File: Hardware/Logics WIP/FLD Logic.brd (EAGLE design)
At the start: 61.6 x 33 mm, 82 parts

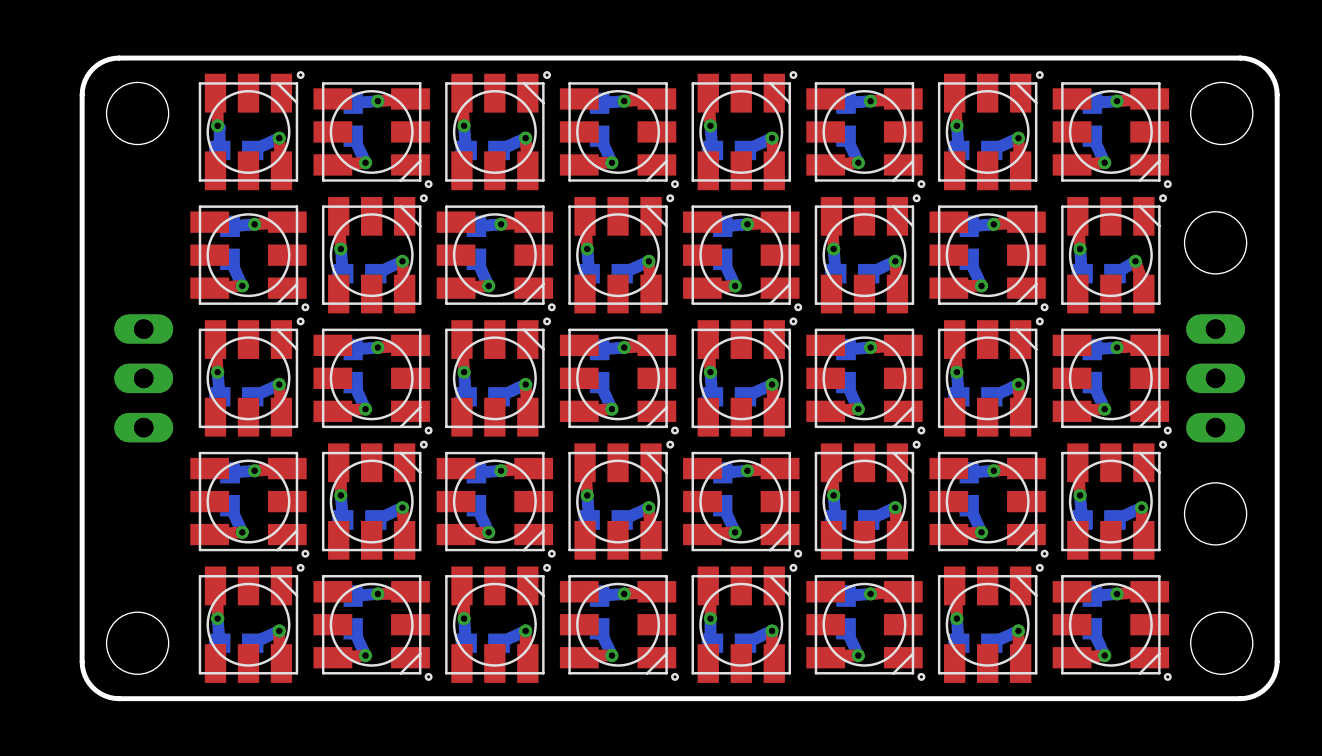
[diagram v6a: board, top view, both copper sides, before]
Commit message: 
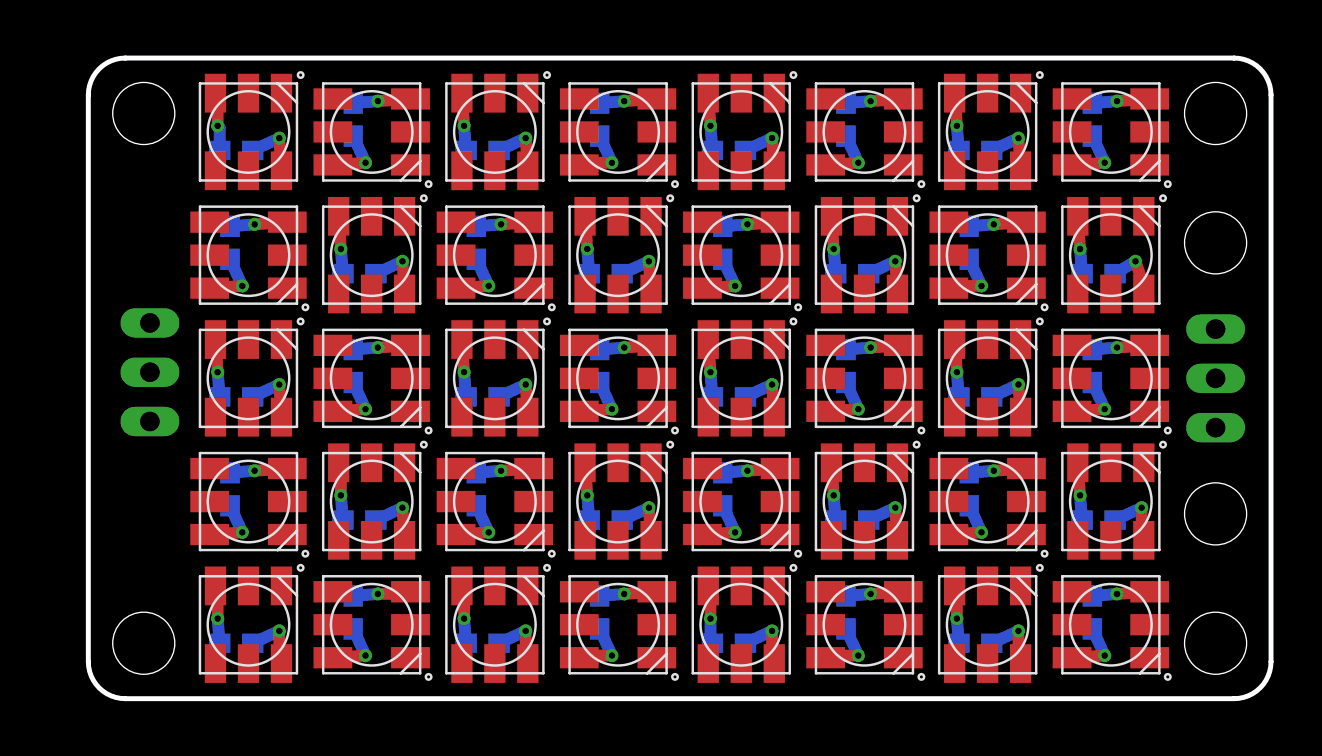
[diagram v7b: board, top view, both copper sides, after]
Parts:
- added U$1: (no value), rseries:RSERIES-OSHW-LOGO-SMALL
- moved OUT 0.45 mm to (3.49, 16.8)
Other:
- board size 61.6 x 33 mm -> 61 x 33 mm
- board text added: "`VULCAN' FRONT LOGIC DISPLAY 2013-08-28"
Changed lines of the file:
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@@
 <setting verticaltext="up"/>
 </settings>
-<grid distance="0.025" unitdist="inch" unit="inch" style="lines" multiple="1" display="yes" altdistance="0.025" altunitdist="inch" altunit="inch"/>
+<grid distance="0.0125" unitdist="inch" unit="inch" style="lines" multiple="1" display="yes" altdistance="0.025" altunitdist="inch" altunit="inch"/>
 <layers>
 <layer number="1" name="Top" color="4" fill="1" visible="yes" active="yes"/>
@@
 <layer number="37" name="tTest" color="7" fill="1" visible="yes" active="yes"/>
 <layer number="38" name="bTest" color="7" fill="1" visible="yes" active="yes"/>
+<layer number="39" name="tKeepout" color="4" fill="11" visible="yes" active="yes"/>
 <layer number="40" name="bKeepout" color="1" fill="11" visible="yes" active="yes"/>
+<layer number="41" name="tRestrict" color="4" fill="10" visible="yes" active="yes"/>
+<layer number="42" name="bRestrict" color="1" fill="10" visible="yes" active="yes"/>
+<layer number="43" name="vRestrict" color="2" fill="10" visible="yes" active="yes"/>
 <layer number="44" name="Drills" color="7" fill="1" visible="yes" active="yes"/>
 <layer number="45" name="Holes" color="7" fill="1" visible="yes" active="yes"/>
@@
 <layer number="106" name="bPlate" color="7" fill="1" visible="yes" active="yes"/>
 <layer number="107" name="Crop" color="7" fill="1" visible="yes" active="yes"/>
+<layer number="108" name="fp8" color="7" fill="1" visible="yes" active="yes"/>
+<layer number="109" name="fp9" color="7" fill="1" visible="yes" active="yes"/>
+<layer number="110" name="fp0" color="7" fill="1" visible="yes" active="yes"/>
+<layer number="111" name="LPC17xx" color="7" fill="1" visible="yes" active="yes"/>
 <layer number="112" name="tSilk" color="7" fill="1" visible="yes" active="yes"/>
 <layer number="116" name="Patch_BOT" color="9" fill="4" visible="yes" active="yes"/>
+<layer number="121" name="_tsilk" color="7" fill="1" visible="yes" active="yes"/>
+<layer number="122" name="_bsilk" color="7" fill="1" visible="yes" active="yes"/>
+<layer number="123" name="tTestmark" color="7" fill="1" visible="yes" active="yes"/>
+<layer number="124" name="bTestmark" color="7" fill="1" visible="yes" active="yes"/>
+<layer number="125" name="_tNames" color="7" fill="1" visible="yes" active="yes"/>
+<layer number="131" name="tAdjust" color="7" fill="1" visible="yes" active="yes"/>
+<layer number="132" name="bAdjust" color="7" fill="1" visible="yes" active="yes"/>
+<layer number="144" name="Drill_legend" color="7" fill="1" visible="yes" active="yes"/>
 <layer number="150" name="Notes" color="7" fill="1" visible="yes" active="yes"/>
+<layer number="151" name="HeatSink" color="7" fill="1" visible="yes" active="yes"/>
 <layer number="153" name="FabDoc1" color="6" fill="1" visible="no" active="no"/>
 <layer number="154" name="FabDoc2" color="2" fill="1" visible="no" active="no"/>
 <layer number="155" name="FabDoc3" color="7" fill="15" visible="no" active="no"/>
+<layer number="199" name="Contour" color="7" fill="1" visible="yes" active="yes"/>
+<layer number="200" name="200bmp" color="1" fill="10" visible="yes" active="yes"/>
+<layer number="201" name="201bmp" color="2" fill="10" visible="yes" active="yes"/>
+<layer number="202" name="202bmp" color="3" fill="10" visible="yes" active="yes"/>
+<layer number="203" name="203bmp" color="4" fill="10" visible="yes" active="yes"/>
+<layer number="204" name="204bmp" color="5" fill="10" visible="yes" active="yes"/>
+<layer number="205" name="205bmp" color="6" fill="10" visible="yes" active="yes"/>
+<layer number="206" name="206bmp" color="7" fill="10" visible="yes" active="yes"/>
+<layer number="207" name="207bmp" color="8" fill="10" visible="yes" active="yes"/>
+<layer number="208" name="208bmp" color="9" fill="10" visible="yes" active="yes"/>
+<layer number="209" name="209bmp" color="7" fill="1" visible="yes" active="yes"/>
+<layer number="210" name="210bmp" color="7" fill="1" visible="yes" active="yes"/>
+<layer number="211" name="211bmp" color="7" fill="1" visible="yes" active="yes"/>
+<layer number="212" name="212bmp" color="7" fill="1" visible="yes" active="yes"/>
+<layer number="213" name="213bmp" color="7" fill="1" visible="yes" active="yes"/>
+<layer number="214" name="214bmp" color="7" fill="1" visible="yes" active="yes"/>
+<layer number="215" name="215bmp" color="7" fill="1" visible="yes" active="yes"/>
+<layer number="216" name="216bmp" color="7" fill="1" visible="yes" active="yes"/>
 <layer number="217" name="217bmp" color="18" fill="1" visible="no" active="no"/>
 <layer number="218" name="218bmp" color="19" fill="1" visible="no" active="no"/>
@@
 <layer number="250" name="Descript" color="3" fill="1" visible="no" active="no"/>
 <layer number="251" name="SMDround" color="12" fill="11" visible="no" active="no"/>
+<layer number="254" name="cooling" color="7" fill="1" visible="yes" active="yes"/>
 </layers>
 <board>
 <plain>
-<wire x1="0" y1="1.905" x2="0" y2="31.115" width="0.254" layer="20"/>
-<wire x1="0" y1="31.115" x2="1.905" y2="33.02" width="0.254" layer="20" curve="-90"/>
-<wire x1="1.905" y1="33.02" x2="59.69" y2="33.02" width="0.254" layer="20"/>
-<wire x1="59.69" y1="33.02" x2="61.595" y2="31.115" width="0.254" layer="20" curve="-90"/>
-<wire x1="61.595" y1="31.115" x2="61.595" y2="1.905" width="0.254" layer="20"/>
-<wire x1="61.595" y1="1.905" x2="59.69" y2="0" width="0.254" layer="20" curve="-90"/>
-<wire x1="59.69" y1="0" x2="1.905" y2="0" width="0.254" layer="20"/>
-<wire x1="1.905" y1="0" x2="0" y2="1.905" width="0.254" layer="20" curve="-90"/>
-<hole x="58.7375" y="30.1625" drill="3.2"/>
-<hole x="58.7375" y="2.8575" drill="3.2"/>
-<hole x="2.8575" y="2.8575" drill="3.2"/>
-<hole x="2.8575" y="30.1625" drill="3.2"/>
+<wire x1="0.3175" y1="1.905" x2="0.3175" y2="31.115" width="0.254" layer="20"/>
+<wire x1="0.3175" y1="31.115" x2="2.2225" y2="33.02" width="0.254" layer="20" curve="-90"/>
+<wire x1="2.2225" y1="33.02" x2="59.3725" y2="33.02" width="0.254" layer="20"/>
+<wire x1="59.3725" y1="33.02" x2="61.2775" y2="31.115" width="0.254" layer="20" curve="-90"/>
+<wire x1="61.2775" y1="31.115" x2="61.2775" y2="1.905" width="0.254" layer="20"/>
+<wire x1="61.2775" y1="1.905" x2="59.3725" y2="0" width="0.254" layer="20" curve="-90"/>
+<wire x1="59.3725" y1="0" x2="2.2225" y2="0" width="0.254" layer="20"/>
+<wire x1="2.2225" y1="0" x2="0.3175" y2="1.905" width="0.254" layer="20" curve="-90"/>
+<hole x="58.42" y="30.1625" drill="3.2"/>
+<hole x="58.42" y="2.8575" drill="3.2"/>
+<hole x="3.175" y="2.8575" drill="3.2"/>
+<hole x="3.175" y="30.1625" drill="3.2"/>
 <hole x="58.42" y="9.525" drill="3.2"/>
 <hole x="58.42" y="23.495" drill="3.2"/>
 <text x="61.2775" y="19.84375" size="1.397" layer="26" font="vector" rot="MR270">+ -</text>
-<text x="1.5875" y="19.84375" size="1.397" layer="26" font="vector" rot="MR270">+ -</text>
+<text x="1.905" y="20.16125" size="1.397" layer="26" font="vector" rot="MR270">+ -</text>
+<text x="26.9875" y="25.4" size="1.016" layer="122" font="vector" rot="MR0" align="center">`VULCAN' FRONT LOGIC DISPLAY
+2013-08-28</text>
 </plain>
 <attributes>
@@
 <element name="C39" library="adafruit" package="C0603" value="0.1uF" x="13.97" y="29.845" smashed="yes" rot="MR270"/>
 <element name="C40" library="adafruit" package="C0603" value="0.1uF" x="7.9375" y="28.2575" smashed="yes" rot="MR180"/>
-<element name="OUT" library="pinhead" package="1X03" value="" x="3.175" y="16.51" smashed="yes" rot="MR270">
-<attribute name="NAME" x="1.5113" y="12.4587" size="1.016" layer="26" font="vector" ratio="10" rot="MR180"/>
-<attribute name="VALUE" x="6.35" y="20.32" size="1.27" layer="28" rot="MR270"/>
+<element name="OUT" library="pinhead" package="1X03" value="" x="3.4925" y="16.8275" smashed="yes" rot="MR270">
+<attribute name="NAME" x="1.8288" y="12.7762" size="1.016" layer="26" font="vector" ratio="10" rot="MR180"/>
+<attribute name="VALUE" x="6.6675" y="20.6375" size="1.27" layer="28" rot="MR270"/>
 </element>
+<element name="U$1" library="rseries" package="RSERIES-OSHW-LOGO-SMALL" value="" x="6.985" y="27.94" rot="MR270"/>
 </elements>
 <signals>
@@
 <wire x1="10.2725" y1="27.51" x2="12.9225" y2="27.51" width="0" layer="19" extent="1-1"/>
 <wire x1="7.62" y1="22.645" x2="10.2725" y2="27.21" width="0" layer="19" extent="1-16"/>
-<wire x1="3.175" y1="19.05" x2="6.5725" y2="21.16" width="0" layer="19" extent="1-1"/>
+<wire x1="3.4925" y1="19.3675" x2="6.5725" y2="21.16" width="0" layer="19" extent="1-1"/>
 <wire x1="46.8875" y1="2.8575" x2="48.26" y2="3.4925" width="0.6096" layer="16"/>
 <via x="48.26" y="3.4925" extent="1-16" drill="0.3302" diameter="0.254" shape="octagon"/>
@@
 <wire x1="8.5725" y1="14.51" x2="8.89" y2="11.7475" width="0" layer="19" extent="1-1"/>
 <wire x1="7.0875" y1="15.5575" x2="8.5725" y2="14.51" width="0" layer="19" extent="1-16"/>
-<wire x1="3.175" y1="16.51" x2="6.985" y2="16.8275" width="0" layer="19" extent="1-1"/>
+<wire x1="3.4925" y1="16.8275" x2="6.985" y2="16.8275" width="0" layer="19" extent="1-1"/>
 <wire x1="6.8725" y1="5.81" x2="6.5725" y2="10.16" width="0" layer="19" extent="1-1"/>
 <wire x1="6.985" y1="5.08" x2="6.8725" y2="5.81" width="0" layer="19" extent="1-1"/>
@@
 <contactref element="OUT" pad="3"/>
 <contactref element="LED40" pad="DO"/>
-<wire x1="3.175" y1="13.97" x2="10.2725" y2="31.21" width="0" layer="19" extent="1-1"/>
+<wire x1="3.4925" y1="14.2875" x2="10.2725" y2="31.21" width="0" layer="19" extent="1-1"/>
 </signal>
 <signal name="N$1">
@@
 </board>
 </drawing>
+<compatibility>
+<note version="6.3" minversion="6.2.2" severity="warning">
+Since Version 6.2.2 text objects can contain more than one line,
+which will not be processed correctly with this version.
+</note>
+</compatibility>
 </eagle>
